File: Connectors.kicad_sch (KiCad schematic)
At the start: 10 parts, among them J14 200528-0100, J15 200528-0100, J16 200528-0100, J17 1824543, J18 200528-0100, J19 200528-0100, J2 200528-0100, J4 200528-0100, J6 200528-0100, J9 200528-0100

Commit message: Updated version to v2.1
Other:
- company: (none) -> Carnegie Mellon University
- title: (none) -> Argus Mainboard
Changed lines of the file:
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@@
 	(generator_version "8.0")
 	(paper "A4")
+	(title_block
+		(title "Argus Mainboard")
+		(date "2024-11-19")
+		(rev "v2.1")
+		(company "Carnegie Mellon University")
+		(comment 1 "M. Holliday")
+		(comment 2 "N. Khera")
+		(comment 3 "V. Rajesh")
+	)
 	(junction
 		(at 189.23 118.11)

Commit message: v3 partial schematic updates
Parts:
- removed J6: 200528-0100, Argus-Connectors:Molex_200528-0100_1x10-1MP_P1.00mm_Horizontal, symbol Connector_Generic_MountingPin:Conn_01x10_MountingPin
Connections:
- net Jetson_CSn is gone; now on net GND: J16.6 (Pin_6)
- net Jetson_MISO is gone; now on net GND: J16.9 (Pin_9)
- net GND: now also J16.4 (Pin_4); no longer J16.5 (Pin_5)
- net Jetson_EN: now also J16.5 (Pin_5); no longer J16.4 (Pin_4)
- net +3V3 renamed +3V3_P
- net +3V3_P: no longer J15.1 (Pin_1), J15.2 (Pin_2), J16.1 (Pin_1)
- net Jetson_CLK renamed Jetson_RX
- net Jetson_MOSI renamed Jetson_TX
- new net +3V3_M: J15.1 (Pin_1), J15.2 (Pin_2), J16.1 (Pin_1)
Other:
- note added: "TODO: ADD Load switches on 3.3V?"
- note added: "TODO: ADD Load switches on VSYS?"
- note added: "TODO: CHANGE CONNECTOR"
- note removed: "CAMERA"
- moved on the sheet: J14, J15, J16, J17, J18, J19, J2, J4, J9

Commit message: v3 Layout complete
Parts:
- removed J17: 1824543, Argus-Connectors:1823654, symbol Argus-Connectors:1824543
- added J13: 282834-6, Argus-Connectors:TE_282834-6, symbol Connector_Generic:Conn_01x06
- added J18: 200528-0100, Argus-Connectors:Molex_200528-0100_1x10-1MP_P1.00mm_Horizontal, symbol Connector_Generic_MountingPin:Conn_01x10_MountingPin
- renumbered J18 to J10, J4 to J11, J14 to J12, J15 to J5, J16 to J6, J2 to J7, J9 to J8, J19 to J9
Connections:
- net +3V3_M: no longer J6.1 (Pin_1)
- net +3V3_P: now also J10.6 (Pin_6), J11.5 (Pin_5), J12.5 (Pin_5), J6.1 (Pin_1), J7.6 (Pin_6), J8.6 (Pin_6), J9.6 (Pin_6); no longer J10.8 (Pin_8), J11.3 (Pin_3), J12.3 (Pin_3), J7.8 (Pin_8), J8.8 (Pin_8), J9.8 (Pin_8)
- net GND: now also J13.2 (Pin_2), J13.4 (Pin_4), J13.6 (Pin_6), J18.1 (Pin_1), J18.10 (Pin_10), J18.4 (Pin_4), J18.6 (Pin_6), J18.7 (Pin_7), J18.8 (Pin_8), J18.9 (Pin_9), J18.MP (MountPin); no longer J10.6 (Pin_6), J11.5 (Pin_5), J12.5 (Pin_5), J5.10 (Pin_10), J5.8 (Pin_8), J5.9 (Pin_9), J7.6 (Pin_6), J8.6 (Pin_6), J9.6 (Pin_6)
- net I2C0_SCL: now also J12.1 (Pin_1); no longer J11.1 (Pin_1), J5.5 (Pin_5), J6.3 (Pin_3)
- net I2C0_SDA: now also J12.2 (Pin_2); no longer J11.2 (Pin_2), J5.6 (Pin_6), J6.2 (Pin_2)
- net I2C1_SCL: now also J11.1 (Pin_1), J5.5 (Pin_5), J6.3 (Pin_3), J18.3 (Pin_3); no longer J12.1 (Pin_1)
- net I2C1_SDA: now also J11.2 (Pin_2), J5.6 (Pin_6), J6.2 (Pin_2), J18.2 (Pin_2); no longer J12.2 (Pin_2)
- net Jetson_RX: now also J6.7 (Pin_7); no longer J6.8 (Pin_8)
- net Jetson_TX: now also J6.8 (Pin_8); no longer J6.7 (Pin_7)
- net VSYS: now also J13.1 (Pin_1), J13.3 (Pin_3), J13.5 (Pin_5)
- new net COIL_EN: J10.8 (Pin_8), J11.3 (Pin_3), J12.3 (Pin_3), J7.8 (Pin_8), J8.8 (Pin_8), J9.8 (Pin_8)
- new net HEATER0_ON: J5.8 (Pin_8)
- new net HEATER1_ON: J5.9 (Pin_9)
- new net HEATER_ENABLE: J5.10 (Pin_10)
- new net RW_EN: J18.5 (Pin_5)
- no-connect marks 2 -> 0
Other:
- note added: "+X"
- note added: "+Y"
- note added: "+Z"
- note added: "-X"
- note added: "-Y"
- note added: "-Z"
- note added: "Power Out"
- note added: "RW"
- note added: "Reaction Wheel"
- note removed: "TODO: ADD Load switches on 3.3V?"
- note removed: "TODO: ADD Load switches on VSYS?"
- note removed: "TODO: CHANGE CONNECTOR"
- note removed: "X+"
- note removed: "X-"
- note removed: "Y+"
- note removed: "Y-"
- note removed: "Z+"
- note removed: "Z-"

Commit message: Addressed design issues
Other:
- note added: "TODO: MAYBE SWAP I2C ON Z BOARDS"
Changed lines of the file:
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@@
+		)
+	)
+	(text "TODO: MAYBE SWAP I2C ON Z BOARDS"
+		(exclude_from_sim no)
+		(at 58.928 193.294 0)
+		(effects
+			(font
+				(size 2.54 2.54)
+			)
+			(justify left)
 		)
 	)

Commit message: v4.0 Updates
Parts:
- removed J13: 282834-6, Argus-Connectors:TE_282834-6, symbol Connector_Generic:Conn_01x06
- added J14, J15, J16: 282834-2, Argus-Connectors:TE_282834-2, symbol Connector_Generic:Conn_01x02
- added J17, J18, J19: 205338-0002, Connector_Molex:Molex_Pico-Lock_205338-0002_1x02-1MP_P2.00mm_Horizontal, symbol Connector_Generic_MountingPin:Conn_01x02_MountingPin
- J10: renamed from J9; value 200528-0100 -> 1-84952-0; footprint Argus-Connectors:Molex_200528-0100_1x10-1MP_P1.00mm_Horizontal -> Argus-Connectors:CON_522711069_MOL
- J11: renamed from J10; value 200528-0100 -> 1-84952-0; footprint Argus-Connectors:Molex_200528-0100_1x10-1MP_P1.00mm_Horizontal -> Argus-Connectors:CON_522711069_MOL
- J12: renamed from J11; value 200528-0100 -> 1-84952-0; footprint Argus-Connectors:Molex_200528-0100_1x10-1MP_P1.00mm_Horizontal -> Argus-Connectors:CON_522711069_MOL
- J13: renamed from J12; value 200528-0100 -> 1-84952-0; footprint Argus-Connectors:Molex_200528-0100_1x10-1MP_P1.00mm_Horizontal -> Argus-Connectors:CON_522711069_MOL
- J5, J6: value 200528-0100 -> 1-84952-0; footprint Argus-Connectors:Molex_200528-0100_1x10-1MP_P1.00mm_Horizontal -> Argus-Connectors:CON_522711069_MOL
- J7: renamed from J18; value 200528-0100 -> 1-84952-0; footprint Argus-Connectors:Molex_200528-0100_1x10-1MP_P1.00mm_Horizontal -> Argus-Connectors:CON_522711069_MOL
- J8: renamed from J7; value 200528-0100 -> 1-84952-0; footprint Argus-Connectors:Molex_200528-0100_1x10-1MP_P1.00mm_Horizontal -> Argus-Connectors:CON_522711069_MOL
- J9: renamed from J8; value 200528-0100 -> 1-84952-0; footprint Argus-Connectors:Molex_200528-0100_1x10-1MP_P1.00mm_Horizontal -> Argus-Connectors:CON_522711069_MOL
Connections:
- net GND: now also J14.2 (Pin_2), J15.2 (Pin_2), J16.2 (Pin_2), J17.2 (Pin_2), J17.MP (MountPin), J18.2 (Pin_2), J18.MP (MountPin), J19.2 (Pin_2), J19.MP (MountPin); no longer J7.7 (Pin_7), J7.8 (Pin_8), J7.9 (Pin_9)
- net VSYS: now also J14.1 (Pin_1), J15.1 (Pin_1), J16.1 (Pin_1), J17.1 (Pin_1), J18.1 (Pin_1), J19.1 (Pin_1); no longer J10.1 (Pin_1), J10.2 (Pin_2), J10.3 (Pin_3), J11.1 (Pin_1), J11.2 (Pin_2), J11.3 (Pin_3), J12.10 (Pin_10), J12.8 (Pin_8), J12.9 (Pin_9), J13.10 (Pin_10), J13.8 (Pin_8), J13.9 (Pin_9), J8.1 (Pin_1), J8.2 (Pin_2), J8.3 (Pin_3), J9.1 (Pin_1), J9.2 (Pin_2), J9.3 (Pin_3)
- new net RW_MOTOR_ALRM: J7.9 (Pin_9)
- new net RW_MOTOR_FLT: J7.8 (Pin_8)
- new net RW_POWER_FLT: J7.7 (Pin_7)
- new net VCHRG: J10.1 (Pin_1), J10.2 (Pin_2), J10.3 (Pin_3), J11.1 (Pin_1), J11.2 (Pin_2), J11.3 (Pin_3), J12.10 (Pin_10), J12.8 (Pin_8), J12.9 (Pin_9), J13.10 (Pin_10), J13.8 (Pin_8), J13.9 (Pin_9), J8.1 (Pin_1), J8.2 (Pin_2), J8.3 (Pin_3), J9.1 (Pin_1), J9.2 (Pin_2), J9.3 (Pin_3)
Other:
- note removed: "RW"
- moved on the sheet: J10, J11, J12, J13, J5, J6, J7, J8, J9

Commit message: DFM updates
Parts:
- J10, J11, J12, J13, J5, J6, J7, J9: value 1-84952-0 -> 522711069; MPN (none) -> C588180
- J14, J15, J16: now left out of the parts list
- J17, J18, J19: MPN (none) -> C17575002
- J8: value 1-84952-0 -> 522711069
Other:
- note removed: "TODO: MAYBE SWAP I2C ON Z BOARDS"
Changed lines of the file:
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@@
 		)
 	)
-	(text "TODO: MAYBE SWAP I2C ON Z BOARDS"
-		(exclude_from_sim no)
-		(at 44.958 184.404 0)
-		(effects
-			(font
-				(size 2.54 2.54)
-			)
-			(justify left)
-		)
-	)
 	(text "Jetson"
 		(exclude_from_sim no)
@@
 			)
 		)
+		(property "MPN" "C17575002"
+			(at 247.65 57.15 0)
+			(effects
+				(font
+					(size 1.27 1.27)
+				)
+				(hide yes)
+			)
+		)
 		(pin "2"
 		)
@@
 			)
 		)
+		(property "MPN" "C17575002"
+			(at 224.79 57.15 0)
+			(effects
+				(font
+					(size 1.27 1.27)
+				)
+				(hide yes)
+			)
+		)
 		(pin "2"
 		)
@@
 			)
 		)
-		(property "Value" "1-84952-0"
+		(property "Value" "522711069"
 			(at 46.99 94.488 0)
 			(effects
@@
 			)
 		)
-		(property "Value" "1-84952-0"
+		(property "Value" "522711069"
 			(at 199.39 94.488 0)
 			(effects
@@
 			)
 		)
+		(property "MPN" "C588180"
+			(at 199.39 107.95 0)
+			(effects
+				(font
+					(size 1.27 1.27)
+				)
+				(hide yes)
+			)
+		)
 		(pin "1"
 		)
@@
 			)
 		)
-		(property "Value" "1-84952-0"
+		(property "Value" "522711069"
 			(at 97.79 94.488 0)
 			(effects
@@
 			)
 		)
+		(property "MPN" "C588180"
+			(at 97.79 107.95 0)
+			(effects
+				(font
+					(size 1.27 1.27)
+				)
+				(hide yes)
+			)
+		)
 		(pin "1"
 		)
@@
 			)
 		)
-		(property "Value" "1-84952-0"
+		(property "Value" "522711069"
 			(at 46.99 143.764 0)
 			(effects
@@
 			)
 		)
+		(property "MPN" "C588180"
+			(at 46.99 157.48 0)
+			(effects
+				(font
+					(size 1.27 1.27)
+				)
+				(hide yes)
+			)
+		)
 		(pin "1"
 		)
@@
 			)
 		)
-		(property "Value" "1-84952-0"
+		(property "Value" "522711069"
 			(at 46.99 34.798 0)
 			(effects
@@
 			)
 		)
+		(property "MPN" "C588180"
+			(at 46.99 48.26 0)
+			(effects
+				(font
+					(size 1.27 1.27)
+				)
+				(hide yes)
+			)
+		)
 		(pin "1"
 		)
@@
 			)
 		)
-		(property "Value" "1-84952-0"
+		(property "Value" "522711069"
 			(at 97.79 34.798 0)
 			(effects
@@
 			)
 		)
+		(property "MPN" "C588180"
+			(at 97.79 48.26 0)
+			(effects
+				(font
+					(size 1.27 1.27)
+				)
+				(hide yes)
+			)
+		)
 		(pin "1"
 		)
@@
 			)
 		)
+		(property "MPN" "C17575002"
+			(at 200.66 57.15 0)
+			(effects
+				(font
+					(size 1.27 1.27)
+				)
+				(hide yes)
+			)
+		)
 		(pin "2"
 		)
@@
 			)
 		)
-		(property "Value" "1-84952-0"
+		(property "Value" "522711069"
 			(at 148.59 94.742 0)
 			(effects
@@
 			)
 		)
+		(property "MPN" "C588180"
+			(at 148.59 107.95 0)
+			(effects
+				(font
+					(size 1.27 1.27)
+				)
+				(hide yes)
+			)
+		)
 		(pin "1"
 		)
@@
 			)
 		)
-		(property "Value" "1-84952-0"
+		(property "Value" "522711069"
 			(at 97.79 143.764 0)
 			(effects
@@
 			)
 		)
+		(property "MPN" "C588180"
+			(at 97.79 157.48 0)
+			(effects
+				(font
+					(size 1.27 1.27)
+				)
+				(hide yes)
+			)
+		)
 		(pin "1"
 		)
@@
 		(unit 1)
 		(exclude_from_sim no)
-		(in_bom yes)
+		(in_bom no)
 		(on_board yes)
 		(dnp yes)
@@
 			)
 		)
-		(property "Value" "1-84952-0"
+		(property "Value" "522711069"
 			(at 148.59 34.798 0)
 			(effects
@@
 			)
 		)
+		(property "MPN" "C588180"
+			(at 148.59 48.26 0)
+			(effects
+				(font
+					(size 1.27 1.27)
+				)
+				(hide yes)
+			)
+		)
 		(pin "1"
 		)
@@
 		(unit 1)
 		(exclude_from_sim no)
-		(in_bom yes)
+		(in_bom no)
 		(on_board yes)
 		(dnp yes)
@@
 		(unit 1)
 		(exclude_from_sim no)
-		(in_bom yes)
+		(in_bom no)
 		(on_board yes)
 		(dnp yes)

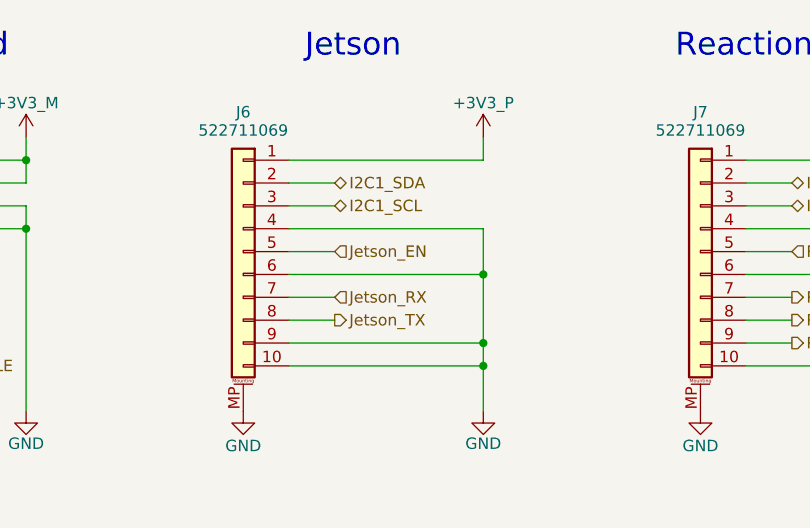
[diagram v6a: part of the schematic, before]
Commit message: Fixed Jetson FPC pinout
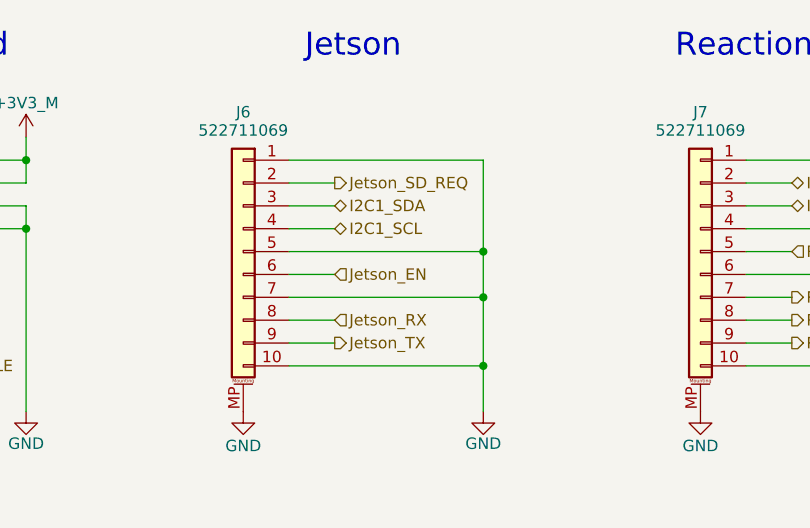
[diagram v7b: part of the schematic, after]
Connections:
- net +3V3_P: no longer J6.1 (Pin_1)
- net GND: now also J6.1 (Pin_1), J6.5 (Pin_5), J6.7 (Pin_7); no longer J6.4 (Pin_4), J6.6 (Pin_6), J6.9 (Pin_9)
- net I2C1_SCL: now also J6.4 (Pin_4); no longer J6.3 (Pin_3)
- net I2C1_SDA: now also J6.3 (Pin_3); no longer J6.2 (Pin_2)
- net Jetson_EN: now also J6.6 (Pin_6); no longer J6.5 (Pin_5)
- net Jetson_RX: now also J6.8 (Pin_8); no longer J6.7 (Pin_7)
- net Jetson_TX: now also J6.9 (Pin_9); no longer J6.8 (Pin_8)
- new net Jetson_SD_REQ: J6.2 (Pin_2)
